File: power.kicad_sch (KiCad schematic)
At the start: 0 parts

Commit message: [#56643] Create buses for interfaces, assign buses to blocks
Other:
- company: (none) -> Antmicro Ltd.
- title: (none) -> Com Express 7 baseboard
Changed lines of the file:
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@@
 (kicad_sch (version 20230121) (generator eeschema)
-  (paper "A4")
+  (paper "A3")
+  (title_block
+    (title "Com Express 7 baseboard")
+    (date "2024-03-22")
+    (rev "1.0.0")
+    (company "Antmicro Ltd.")
+  )
 )

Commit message: [#58137] Add DC/DC supplies
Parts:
- added C174, C180, C190, C195: C_Pol_100u_10V_KEMET-T520-B, antmicro-footprints:C_Pol_EIA-B, symbol antmicroCapacitorspol:C_Pol_100u_10V_KEMET-T520-B
- added C175, C177, C179, C181, C183, C184, C192, C194, C196, C197, C198, C199, C200: C_1u_0402, antmicro-footprints:C_0402_1005Metric, symbol antmicroCapacitors0402:C_1u_0402
- added C178, C186, C188, C189, C191, C57: C_22u_16V_0603, antmicro-footprints:C_0603_1608Metric, symbol antmicroCapacitors0603:C_22u_16V_0603
- added C182, C193: C_100n_0402, antmicro-footprints:C_0402_1005Metric, symbol antmicroCapacitors0402:C_100n_0402
- added C185, C187, C201: C_Pol_68u_16V_Panasonic-TQC-D, antmicro-footprints:C_Pol_EIA-D, symbol antmicroCapacitorspol:C_Pol_68u_16V_Panasonic-TQC-D
- added F2: F_12A_1206, antmicro-footprints:F_1206_3216Metric, symbol antmicroFuses:F_12A_1206
- added J13: Molex_Nano-Fit_1x2_105309-2202, antmicro-footprints:Conn_Molex_Nano-Fit_1x2_105309-2202, symbol antmicroWire2BoardConnectors:Molex_Nano-Fit_1x2_105309-2202
- added L1, L2, L3: L_1u8_6.8A_WE-MAPI-4020, antmicro-footprints:L_WE-MAPI-4020, symbol antmicroFixedInductors:L_1u8_6.8A_WE-MAPI-4020
- added L4: L_1u8_14A_Coilcraft-XAL6030, antmicro-footprints:L_Coilcraft-XAL6030, symbol antmicroFixedInductors:L_1u8_14A_Coilcraft-XAL6030
- added Q6: SSM3J332R, antmicro-footprints:SOT-23-3, symbol antmicroTransistorsFETsMOSFETsSingle:SSM3J332R
- added R289, R290, R294, R298: R_15k_0402, antmicro-footprints:R_0402_1005Metric, symbol antmicroResistors0402:R_15k_0402
- added R291, R296, R85: R_10k_0402, antmicro-footprints:R_0402_1005Metric, symbol antmicroResistors0402:R_10k_0402
- added R292, R295, R297: R_68k_0402, antmicro-footprints:R_0402_1005Metric, symbol antmicroResistors0402:R_68k_0402
- added R293: R_110k_0402, antmicro-footprints:R_0402_1005Metric, symbol antmicroResistors0402:R_110k_0402
- added R299, R300, R302, R303, R306: R_0R001_0805, antmicro-footprints:R_0805_2012Metric, symbol antmicroResistorsmisc:R_0R001_0805
- added R301: R_0R_0402, antmicro-footprints:R_0402_1005Metric, symbol antmicroResistors0402:R_0R_0402
- added R86: R_30k_0402, antmicro-footprints:R_0402_1005Metric, symbol antmicroResistors0402:R_30k_0402
- added U46, U50: TPS564247DRLR, symbol antmicroDCDCConverters:TPS564247DRLR
- added U47, U48: TPS56C230, antmicro-footprints:QFN-20-1EP_3x3mm_P0.45mm, symbol antmicroDCDCConverters:TPS56C230
- added U49: TLV73333PDBVT, antmicro-footprints:SOT-23-5, symbol antmicroPMICVoltageRegulatorsLinear:TLV73333PDBVT
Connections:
- new net: R298.2, R86.1, U50.6 (FB)
- new net: C193.2, L4.1, U48.19 (SW), U48.20 (SW), U48.6 (SW)
- new net: C194.2, C195.1, L4.2, R297.2, R302.1
- new net: C192.2, R295.2, U48.17 (V_{CC})
- new net: C184.2, C190.1, L3.2, R300.1, R85.2
- new net: L2.1, U46.2 (SW)
- new net: C179.2, C180.1, L2.2, R293.2, R303.1
- new net: C182.2, L3.1, U47.19 (SW), U47.20 (SW), U47.6 (SW)
- new net: R291.2, R292.1, U47.15 (MODE)
- new net: C183.2, R292.2, U47.17 (V_{CC})
- new net: C174.1, C175.2, L1.2, R306.1, R86.2
- new net: L1.1, U50.2 (SW)
- new net: C198.2, R301.1, U49.5 (VOUT)
- new net: R289.2, R297.1, U48.14 (FB)
- new net: R290.2, R85.1, U47.14 (FB)
- new net: R293.1, R294.2, U46.6 (FB)
- new net: C193.1, U48.1 (BST)
- new net: R295.1, R296.2, U48.15 (MODE)
- new net: F2.2, R299.1
- new net: C182.1, U47.1 (BST)
- new net +12V: C178.2, C185.1, C186.2, C187.1, C188.2, C189.2, C191.2, C201.1, C57.2, R299.2, U46.1 (V_{IN}), U47.2 (V_{IN}), U47.3 (V_{IN}), U47.4 (V_{IN}), U47.5 (V_{IN}), U48.2 (V_{IN}), U48.3 (V_{IN}), U48.4 (V_{IN}), U48.5 (V_{IN}), U50.1 (V_{IN})
- new net +1V0: C199.2, R300.2
- new net +1V8: C177.2, R306.2
- new net +3V3: C196.2, R302.2
- new net +3V3_AON: R301.2
- new net +5V: C181.2, Q6.3 (D)
- new net +5V_AON: C197.2, C200.2, Q6.2 (S), R303.2, U49.1 (VIN), U49.3 (EN)
- new net GND: C174.2, C175.1, C177.1, C178.1, C179.1, C180.2, C181.1, C183.1, C184.1, C185.2, C186.1, C187.2, C188.1, C189.1, C190.2, C191.1, C192.1, C194.1, C195.2, C196.1, C197.1, C198.1, C199.1, C200.1, C201.2, C57.1, J13.2, R289.1, R290.1, R291.1, R294.1, R296.1, R298.1, U46.2 (SW), U46.4 (AGND), U47.13 (AGND), U47.18 (PGND), U47.21 (PGND), U47.7 (PGND), U47.8 (PGND), U48.13 (AGND), U48.18 (PGND), U48.21 (PGND), U48.7 (PGND), U48.8 (PGND), U49.2 (GND), U50.2 (SW), U50.4 (AGND)
- new net VCC: F2.1, J13.1
- no-connect marks 0 -> 2
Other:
- note added: "+12V SOURCE AND BULK DECOUPLING"
- note added: "+1V0 DC/DC CONVERTER"
- note added: "+1V8 DC/DC CONVERTER"
- note added: "+3V3_AON LDO"
- note added: "+5V DC/DC CONVERTER"
- note added: "Backplane is responsible for backfeed protection"
- note added: "From backplane connector"
- note added: "V_{out} = 1.0 V f_{SW} = 500 kHz I_{L} = 5.5 A ΔI_{L} = 19% I_{Lpeak} = 6.02 A"
- note added: "V_{out} = 1.8 V f_{SW} = 1200 kHz I_{L} = 1.0 A ΔI_{L} = 71% I_{Lpeak} = 1.35 A"
- note added: "V_{out} = 3.3 V f_{SW} = 500 kHz I_{L} = 11.0 A ΔI_{L} = 25% I_{Lpeak} = 12.4 A"
- note added: "V_{out} = 5.0 V f_{SW} = 1200 kHz I_{L} = 4.0 A ΔI_{L} = 34% I_{Lpeak} = 4.68 A"

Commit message: [#58137] Add power sequencing and reset
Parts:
- added C202: C_1u_0402, antmicro-footprints:C_0402_1005Metric, symbol antmicroCapacitors0402:C_1u_0402
- added C203, C205: C_100n_0402, antmicro-footprints:C_0402_1005Metric, symbol antmicroCapacitors0402:C_100n_0402
- added C204: C_68n_0402, antmicro-footprints:C_0402_1005Metric, symbol antmicroCapacitors0402:C_68n_0402
- added Q5: SI7613DN-T1-GE3, antmicro-footprints:Vishay_PowerPAK_1212-8_Single, symbol antmicroTransistorsFETsMOSFETsSingle:SI7613DN-T1-GE3
- added Q7, Q8: BSS138-7-F, antmicro-footprints:SOT-23-3, symbol antmicroTransistorsFETsMOSFETsSingle:BSS138-7-F
- added R222: R_15k_0402, antmicro-footprints:R_0402_1005Metric, symbol antmicroResistors0402:R_15k_0402
- added R245, R309, R314, R315, R317: R_10k_0402, antmicro-footprints:R_0402_1005Metric, symbol antmicroResistors0402:R_10k_0402
- added R246, R310, R311, R318: R_0R_0402, antmicro-footprints:R_0402_1005Metric, symbol antmicroResistors0402:R_0R_0402
- added R251, R307, R308, R313: R_100k_0402, antmicro-footprints:R_0402_1005Metric, symbol antmicroResistors0402:R_100k_0402
- added R312, R316: R_30k_0402, antmicro-footprints:R_0402_1005Metric, symbol antmicroResistors0402:R_30k_0402
- added R320: R_1k_0402, antmicro-footprints:R_0402_1005Metric, symbol antmicroResistors0402:R_1k_0402
- added U51: TPS3840PL30DBVR, antmicro-footprints:SOT-23-5, symbol antmicroPMICPowerSequencers:TPS3840PL30DBVR
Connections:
- net +12V: now also C202.2, Q5.5 (D), R314.2; no longer C178.2, C185.1, C186.2, C187.1, C188.2, C189.2, C191.2, C201.1, C57.2, R299.2, U46.1 (V_{IN}), U47.2 (V_{IN}), U47.3 (V_{IN}), U47.4 (V_{IN}), U47.5 (V_{IN}), U48.2 (V_{IN}), U48.3 (V_{IN}), U48.4 (V_{IN}), U48.5 (V_{IN}), U50.1 (V_{IN})
- net +1V8: now also R310.1
- net +3V3: now also R317.2
- net +3V3_AON: now also C203.2, U51.2 (VDD)
- net +5V: now also R315.2
- net +5V_AON: now also R313.2
- net GND: now also C202.1, C203.1, C204.1, C205.1, Q7.2 (S), Q8.2 (S), R245.1, R251.1, R308.1, R312.2, R316.2, R320.1, U51.3 (GND)
- net at C192.2, R295.2, U48.17 (V_{CC}): now also R309.2
- net at U50.5 (EN): now also R311.2
- net at U48.12 (EN): now also R315.1, R316.1
- net PG_{5V}: now reaches U48.9 (PG)
- net PG_{5V}: now also R309.1, R311.1
- net at U47.12 (EN): now also R310.2
- net PG_{1V0}: now reaches U47.9 (PG)
- net PG_{1V0}: now also R251.2, R317.1, R318.1
- net at Q6.1 (G): now also Q8.3 (D), R313.1
- net at U46.5 (EN): now also R222.1, R245.2
- new net: Q8.1 (G), R246.2, R312.1, R314.1
- new net: C204.2, C205.2, U51.5 (CT)
- new net: R318.2, U51.4 (~{MR})
- new net: Q5.4 (G), Q7.3 (D), R307.1
- new net +12V_AON: C178.2, C185.1, C186.2, C187.1, C188.2, C189.2, C191.2, C201.1, C57.2, Q5.1 (S), Q5.2 (S), Q5.3 (S), R222.2, R299.2, R307.2, U46.1 (V_{IN}), U47.2 (V_{IN}), U47.3 (V_{IN}), U47.4 (V_{IN}), U47.5 (V_{IN}), U48.2 (V_{IN}), U48.3 (V_{IN}), U48.4 (V_{IN}), U48.5 (V_{IN}), U50.1 (V_{IN})
- new net PSON: Q7.1 (G), R308.2
- new net PWR_OK: R320.2, U51.1 (~{RESET})
- new net ~{RESET}: R246.1
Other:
- note added: "100 ms delay"
- note added: "1V0 is last in PG chain so then if it's PG is high all rails should be OK"
- note added: "PSU rail description: * +12V_{AON} - Input power Always on rails: * +5V_{AON} * +3V3_{AON} Board rails (PSON == 1): * +12V * +5V * +3V3 * +1V8 * +1V0"
- note added: "Sequence: +5V_{AON} +3V3_{AON} *Power button* +12V +5V +3V3 +1V8 +1V0"
- moved on the sheet: C178, C181, C183, C185, C187, C188, C191, C192, C201, C57, F2, J13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

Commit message: Fix ERC
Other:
- moved on the sheet: R316

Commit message: Reannotate schematic
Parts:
- renumbered C187 to C39, C191 to C40, C185 to C41, C188 to C42, C201 to C43, C183 to C44, C192 to C45, C202 to C46, C182 to C47, C193 to C48, C184 to C49, C194 to C50, C190 to C51, C195 to C52, C204 to C53, C203 to C54, C205 to C55, C199 to C56, C196 to C57, C178 to C58, C57 to C59, C186 to C60, C189 to C61, C179 to C62, C175 to C63, C180 to C64, C174 to C65, C197 to C66, C200 to C67, C177 to C68, C198 to C69, C181 to C70, F2 to F1, J13 to J6, L3 to L1, L4 to L2, L2 to L3, L1 to L4, Q7 to Q1, Q5 to Q2, Q8 to Q3, Q6 to Q4, R289 to R100, R251 to R101, R318 to R102, R300 to R103, R302 to R104, R320 to R105, R311 to R106, R222 to R107, R245 to R108, R293 to R109, R294 to R110, R86 to R111, R298 to R112, R303 to R113, R306 to R114, R246 to R115, R314 to R116, R312 to R117, R313 to R118, R301 to R119, R299 to R85, R315 to R86, R316 to R87, R292 to R88, R291 to R89, R308 to R90, R295 to R91, R296 to R92, R310 to R93, R307 to R94, R317 to R95, R309 to R96, R85 to R97, R290 to R98, R297 to R99, U47 to U18, U48 to U19, U51 to U20, U46 to U21, U50 to U22, U49 to U23

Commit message: Optimize BOM, reannotate
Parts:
- removed C53: C_68n_0402, antmicro-footprints:C_0402_1005Metric, symbol antmicroCapacitors0402:C_68n_0402
- added C53: C_100n_0402, antmicro-footprints:C_0402_1005Metric, symbol antmicroCapacitors0402:C_100n_0402
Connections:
- net GND: now also C53.1
- net at C55.2, U20.5 (CT): now also C53.2
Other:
- note added: "~120 ms delay"
- note removed: "100 ms delay"
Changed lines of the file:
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@@
     (effects (font (size 1.27 1.27)) (justify left bottom))
   )
-  (text "100 ms delay" (at 179.07 252.73 0)
+  (text "~120 ms delay" (at 179.07 252.73 0)
     (effects (font (size 1.27 1.27)) (justify left bottom))
   )
@@
     )
   )
-  (symbol (lib_id "antmicroCapacitors0402:C_68n_0402") (at 161.29 254 90) (unit 1)
-    (in_bom yes) (on_board yes) (dnp no) (fields_autoplaced)
-    (property "Reference" "C53" (at 163.83 250.1836 90)
-      (effects (font (size 1.27 1.27) (thickness 0.15)) (justify right))
-    )
-    (property "Value" "C_68n_0402" (at 171.45 233.68 0)
-      (effects (font (size 1.27 1.27) (thickness 0.15)) (justify left bottom) hide)
-    )
-    (property "Footprint" "antmicro-footprints:C_0402_1005Metric" (at 173.99 233.68 0)
-      (effects (font (size 1.27 1.27) (thickness 0.15)) (justify left bottom) hide)
-    )
-    (property "Datasheet" "https://www.yageo.com/en/Chart/Download/pdf/CC402KRX7R7BB683" (at 176.53 233.68 0)
-      (effects (font (size 1.27 1.27) (thickness 0.15)) (justify left bottom) hide)
-    )
-    (property "MPN" "CC402KRX7R7BB683" (at 179.07 233.68 0)
-      (effects (font (size 1.27 1.27) (thickness 0.15)) (justify left bottom) hide)
-    )
-    (property "Manufacturer" "YAGEO" (at 181.61 233.68 0)
-      (effects (font (size 1.27 1.27) (thickness 0.15)) (justify left bottom) hide)
-    )
-    (property "License" "Apache-2.0" (at 184.15 233.68 0)
-      (effects (font (size 1.27 1.27) (thickness 0.15)) (justify left bottom) hide)
-    )
-    (property "Author" "Antmicro" (at 186.69 233.68 0)
-      (effects (font (size 1.27 1.27) (thickness 0.15)) (justify left bottom) hide)
-    )
-    (property "Val" "68n" (at 163.83 252.7236 90)
-      (effects (font (size 1.27 1.27) (thickness 0.15)) (justify right))
-    )
-    (property "Voltage" "" (at 189.23 233.68 0)
-      (effects (font (size 1.27 1.27)) (justify left bottom) hide)
-    )
-    (property "Dielectric" "" (at 191.77 233.68 0)
-      (effects (font (size 1.27 1.27)) (justify left bottom) hide)
-    )
-    (pin "1")
-    (pin "2")
-    (instances
-      (project "com-express-7-baseboard"
-        (path "/1b8c34da-dad5-4b0b-8c4b-45db766c4dfa/9e43a8fe-5590-4346-856e-e8b6e5166965"
-          (reference "C53") (unit 1)
-        )
-      )
-    )
-  )
   (symbol (lib_id "antmicroCapacitors0402:C_1u_0402") (at 393.7 66.04 90) (unit 1)
     (in_bom yes) (on_board yes) (dnp no)
@@
         )
       )
+    )
+  )
+  (symbol (lib_id "antmicroCapacitors0402:C_100n_0402") (at 161.29 254 90) (unit 1)
+    (in_bom yes) (on_board yes) (dnp no) (fields_autoplaced)
+    (property "Reference" "C53" (at 163.83 250.1836 90)
+      (effects (font (size 1.27 1.27) (thickness 0.15)) (justify right))
+    )
+    (property "Value" "C_100n_0402" (at 171.45 233.68 0)
+      (effects (font (size 1.27 1.27) (thickness 0.15)) (justify left bottom) hide)
+    )
+    (property "Footprint" "antmicro-footprints:C_0402_1005Metric" (at 173.99 233.68 0)
+      (effects (font (size 1.27 1.27) (thickness 0.15)) (justify left bottom) hide)
+    )
+    (property "Datasheet" "https://www.murata.com/products/productdetail?partno=GRM155R61H104KE14%23" (at 176.53 233.68 0)
+      (effects (font (size 1.27 1.27) (thickness 0.15)) (justify left bottom) hide)
+    )
+    (property "MPN" "GRM155R61H104KE14D" (at 179.07 233.68 0)
+      (effects (font (size 1.27 1.27) (thickness 0.15)) (justify left bottom) hide)
+    )
+    (property "Manufacturer" "Murata" (at 181.61 233.68 0)
+      (effects (font (size 1.27 1.27) (thickness 0.15)) (justify left bottom) hide)
+    )
+    (property "License" "Apache-2.0" (at 184.15 233.68 0)
+      (effects (font (size 1.27 1.27) (thickness 0.15)) (justify left bottom) hide)
+    )
+    (property "Author" "Antmicro" (at 186.69 233.68 0)
+      (effects (font (size 1.27 1.27) (thickness 0.15)) (justify left bottom) hide)
+    )
+    (property "Val" "100n" (at 163.83 252.7236 90)
+      (effects (font (size 1.27 1.27) (thickness 0.15)) (justify right))
+    )
+    (property "Voltage" "50V" (at 189.23 233.68 0)
+      (effects (font (size 1.27 1.27)) (justify left bottom) hide)
+    )
+    (property "Dielectric" "X5R" (at 191.77 233.68 0)
+      (effects (font (size 1.27 1.27)) (justify left bottom) hide)
+    )
+    (pin "1")
+    (pin "2")
+    (instances
+      (project "com-express-7-baseboard"
+        (path "/1b8c34da-dad5-4b0b-8c4b-45db766c4dfa/9e43a8fe-5590-4346-856e-e8b6e5166965"
+          (reference "C53") (unit 1)
+        )
+      )

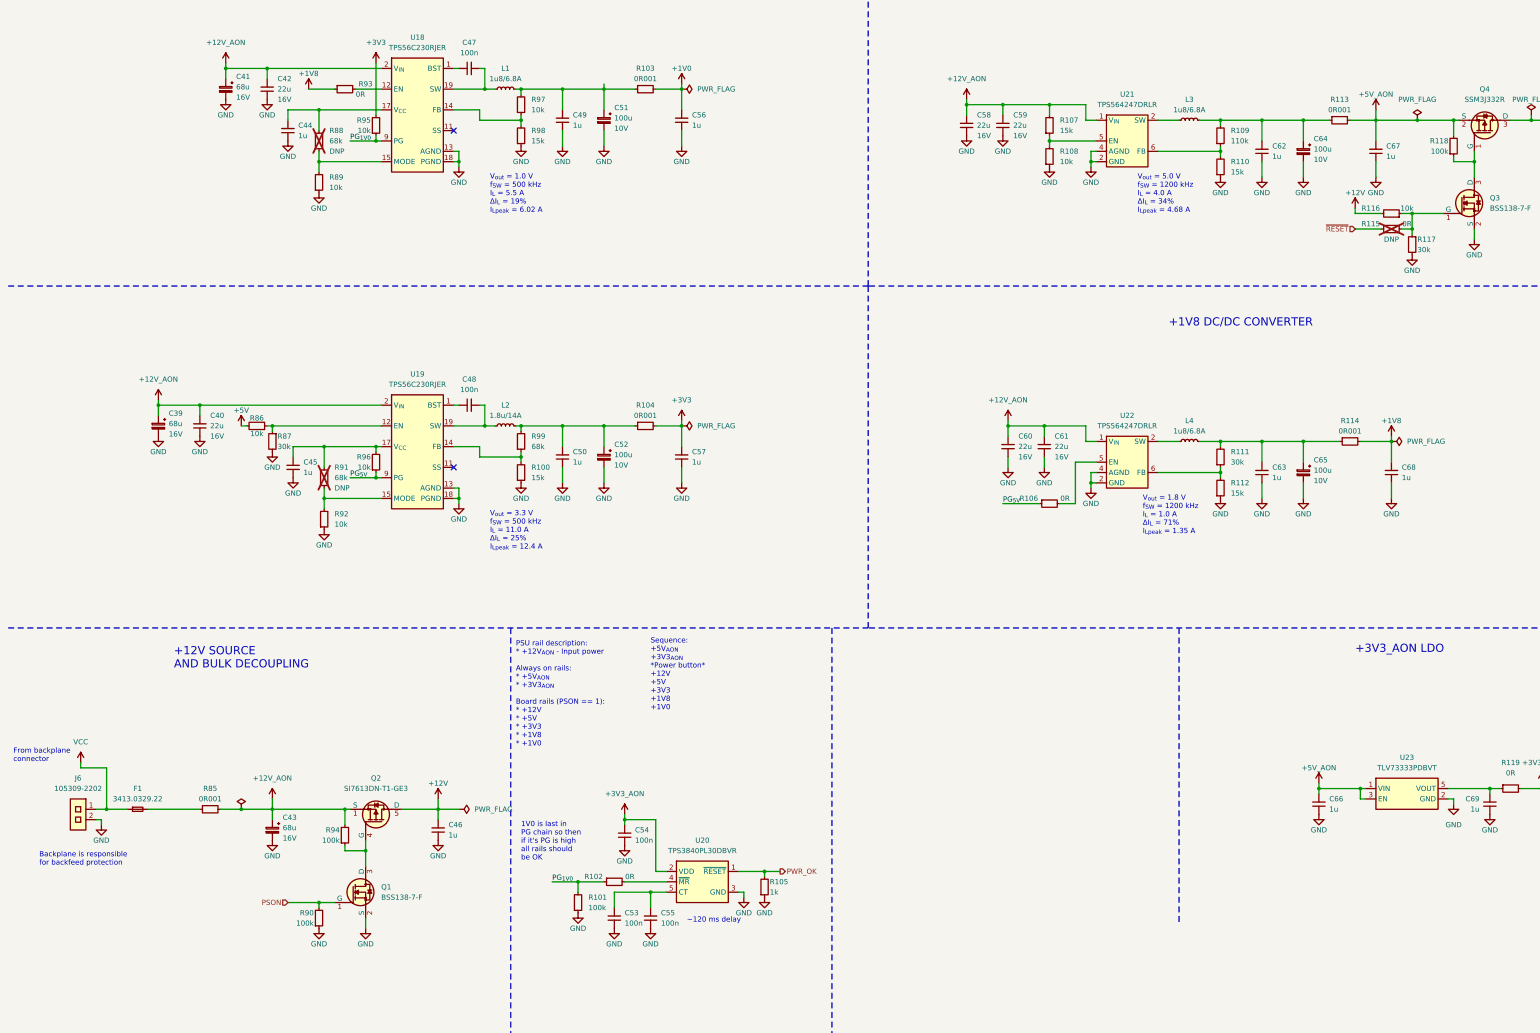
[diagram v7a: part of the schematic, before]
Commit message: [#58137] Add power monitors; clean up I2C bus
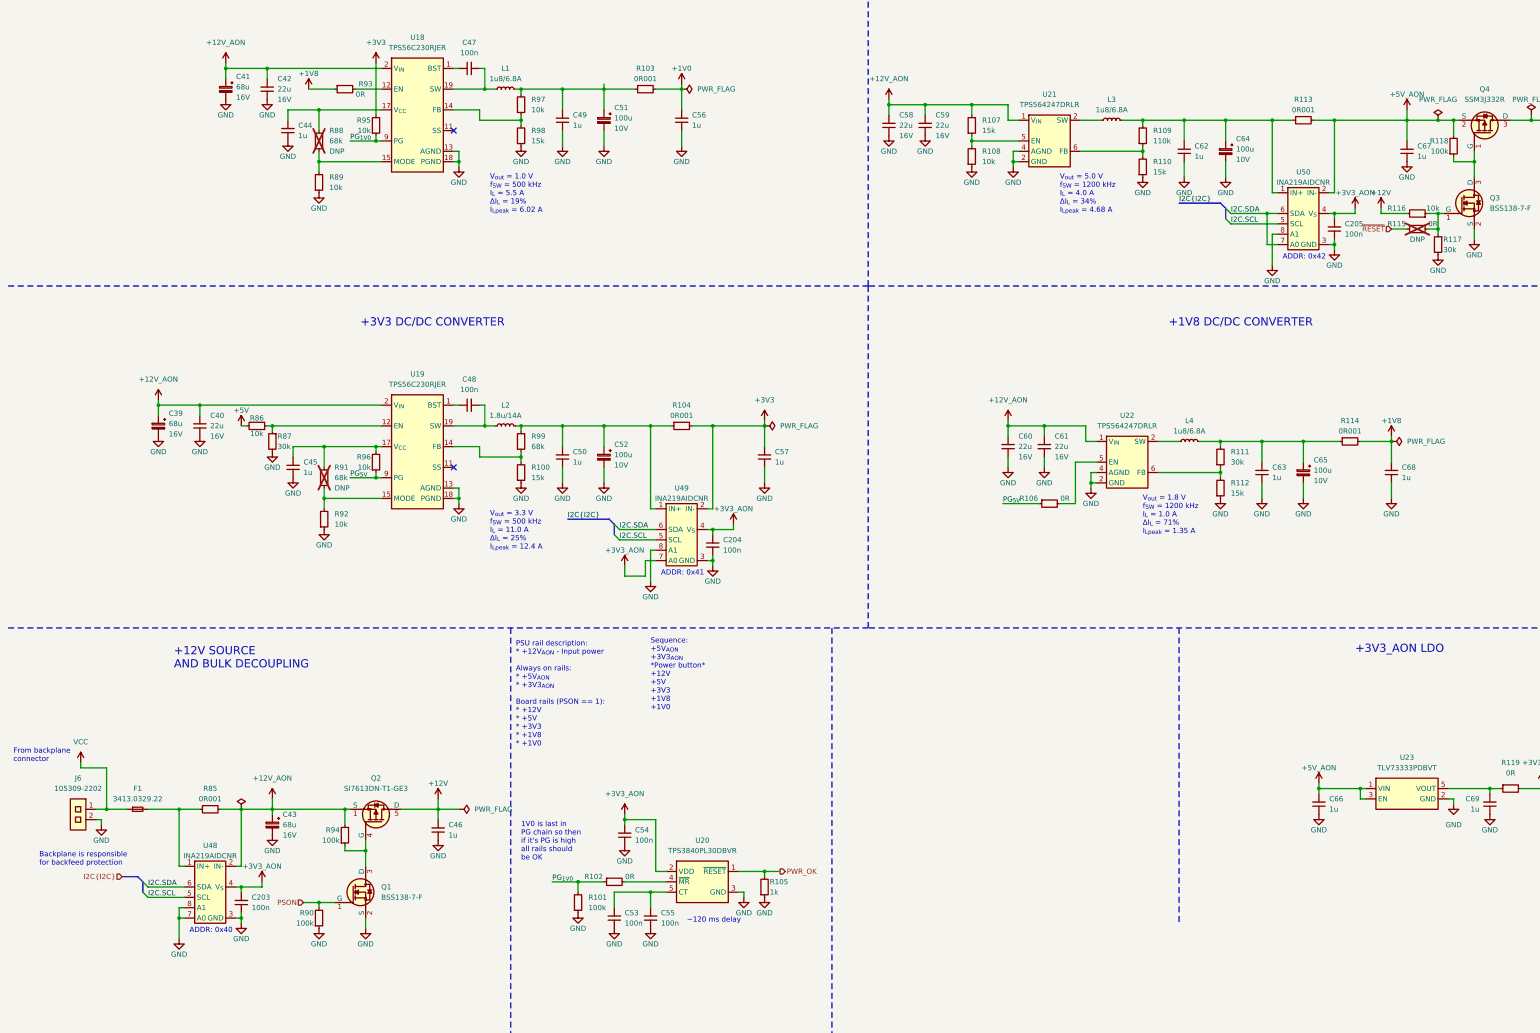
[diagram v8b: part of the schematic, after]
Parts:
- added C203, C204, C205: C_100n_0402, antmicro-footprints:C_0402_1005Metric, symbol antmicroCapacitors0402:C_100n_0402
- added U48, U49, U50: INA219AIDCNR, symbol antmicroPowerMeasurement:INA219AIDCNR
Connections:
- net +12V_AON: now also U48.2 (IN-)
- net +3V3: now also U49.2 (IN-)
- net +3V3_AON: now also C203.2, C204.2, C205.2, U48.4 (V_{S}), U49.4 (V_{S}), U49.7 (A0), U50.4 (V_{S})
- net +5V_AON: now also U50.2 (IN-)
- net GND: now also C203.1, C204.1, C205.1, U48.3 (GND), U48.7 (A0), U48.8 (A1), U49.3 (GND), U49.8 (A1), U50.3 (GND), U50.8 (A1)
- net at C50.2, C52.1, L2.2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: now also U49.1 (IN+)
- net at C62.2, C64.1, L3.2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: now also U50.1 (IN+)
- net at F1.2, R85.1: now also U48.1 (IN+)
- new net I2C.SCL: U48.5 (SCL), U49.5 (SCL), U50.5 (SCL)
- new net I2C.SDA: U48.6 (SDA), U49.6 (SDA), U50.6 (SDA), U50.7 (A0)
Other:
- note added: "+3V3 DC/DC CONVERTER"
- note added: "ADDR: 0x40"
- note added: "ADDR: 0x41"
- note added: "ADDR: 0x42"
- moved on the sheet: C43, C57, C58, C59, C62, C64, C67, L3, R104, R107, R108, R109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
